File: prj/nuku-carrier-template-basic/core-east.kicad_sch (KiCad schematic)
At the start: 1 part, among them J2 DF40HC(4.0)-90DS-0.4V

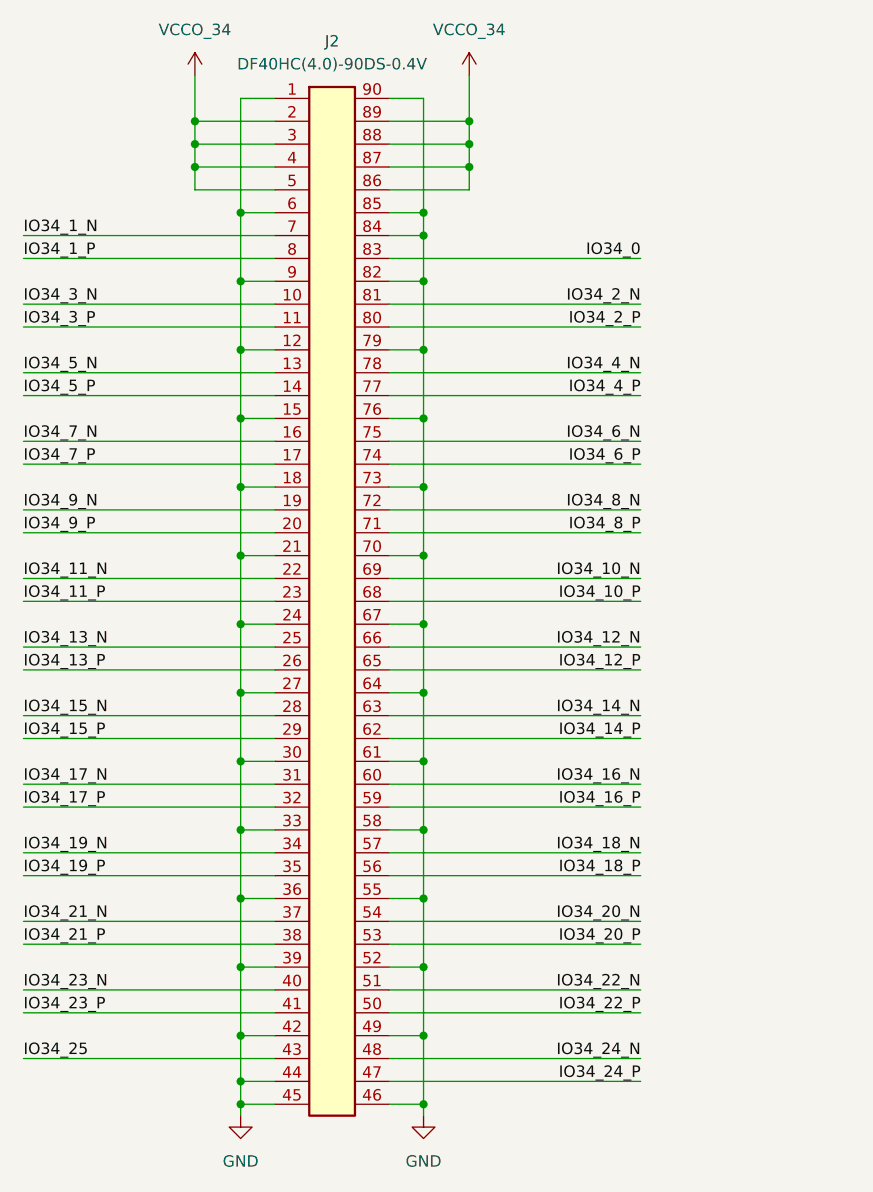
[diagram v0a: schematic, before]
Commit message: Finish template.basic + Production outputs
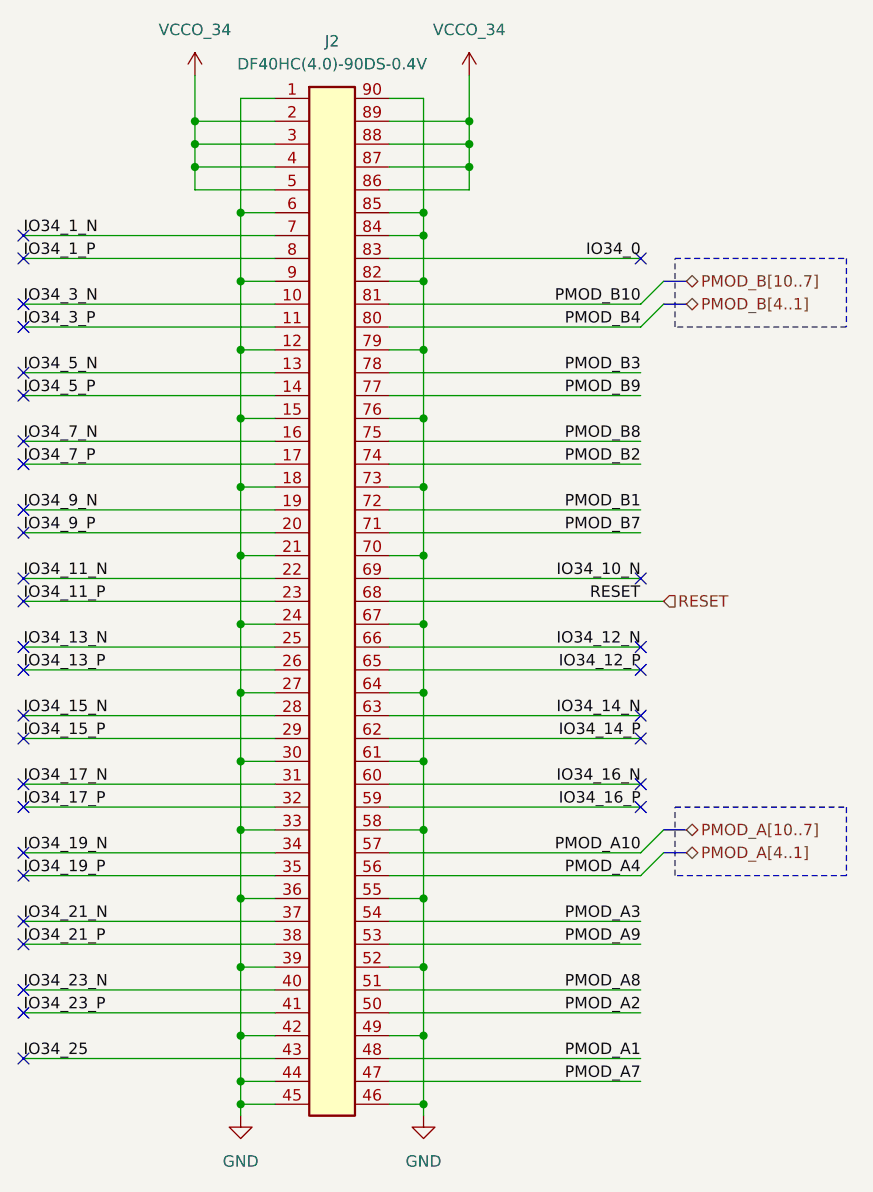
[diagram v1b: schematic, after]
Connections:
- net IO34_10_P renamed RESET
- net IO34_18_N renamed PMOD_A10
- net IO34_18_P renamed PMOD_A4
- net IO34_20_N renamed PMOD_A3
- net IO34_20_P renamed PMOD_A9
- net IO34_22_N renamed PMOD_A8
- net IO34_22_P renamed PMOD_A2
- net IO34_24_N renamed PMOD_A1
- net IO34_24_P renamed PMOD_A7
- net IO34_2_N renamed PMOD_B10
- net IO34_2_P renamed PMOD_B4
- net IO34_4_N renamed PMOD_B3
- net IO34_4_P renamed PMOD_B9
- net IO34_6_N renamed PMOD_B8
- net IO34_6_P renamed PMOD_B2
- net IO34_8_N renamed PMOD_B1
- net IO34_8_P renamed PMOD_B7
- no-connect marks 0 -> 33

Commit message: Finish bridgeless template
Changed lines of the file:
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@@
+	)
+	(rectangle
+		(start 186.69 93.98)
+		(end 196.85 99.06)
+		(stroke
+			(width 0)
+			(type dash)
+		)
+		(fill
+			(type none)
+		)
 	)
 	(rectangle
@@
 	(wire
 		(pts
-			(xy 154.94 96.52) (xy 185.42 96.52)
+			(xy 154.94 96.52) (xy 187.96 96.52)
 		)
 		(stroke
@@
 	(hierarchical_label "RESET"
 		(shape input)
-		(at 185.42 96.52 0)
-		(effects
-			(font
+		(at 187.96 96.52 0)
+		(effects
+			(font

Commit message: Finish boards - prod ready
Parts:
- J2: footprint nuku:DF40HC(4.0)-90DS-0.4V -> nuku:DF40C-90DS-0.4V; symbol nuku:DF40HC(4.0)-90DS-0.4V -> nuku:DF40C-90DS-0.4V; LCSC C597947 -> C2911197
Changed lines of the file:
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@@
 	)
 	(symbol
-		(lib_id "nuku:DF40HC(4.0)-90DS-0.4V")
+		(lib_id "nuku:DF40C-90DS-0.4V")
 		(at 146.05 39.37 0)
 		(unit 1)
@@
 			)
 		)
-		(property "Footprint" "nuku:DF40HC(4.0)-90DS-0.4V"
+		(property "Footprint" "nuku:DF40C-90DS-0.4V"
 			(at 146.05 156.21 0)
 			(effects
@@
 			)
 		)
-		(property "Datasheet" "https://www.lcsc.com/datasheet/lcsc_datasheet_2006112253_HRS-Hirose-DF40HC-4-0-90DS-0-4V-51_C597947.pdf"
+		(property "Datasheet" "https://www.lcsc.com/datasheet/lcsc_datasheet_2206011716_HRS-Hirose-DF40C-90DS-0-4V-51_C2911197.pdf"
 			(at 146.05 158.75 0)
 			(effects
@@
 			)
 		)
-		(property "LCSC" "C597947"
-			(at 146.05 39.37 0)
+		(property "LCSC" "C2911197"
+			(at 146.05 160.02 0)
 			(effects
 				(font
 					(size 1.27 1.27)
 				)
+				(justify left top)
 				(hide yes)
 			)
